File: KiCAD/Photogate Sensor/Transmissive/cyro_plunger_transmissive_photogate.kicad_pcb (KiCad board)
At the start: 2 copper layers, 100 x 100 mm, 0 parts

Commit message: Finish draft of schematic, started on board
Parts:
- added C1: 1µF, Capacitor_SMD:C_0805_2012Metric, F.Cu at (140.8, -2.38)
- added C2: 4.7µF, Capacitor_SMD:C_0805_2012Metric, F.Cu at (140.8, 0.63)
- added C3: 100nF, Capacitor_SMD:C_0805_2012Metric, F.Cu at (140.8, 3.64)
- added C4: 100nF, Capacitor_SMD:C_0805_2012Metric, F.Cu at (27.8, 25.0)
- added C5: 100nF, Capacitor_SMD:C_0805_2012Metric, F.Cu at (140.8, 9.66)
- added C6: 100nF, Capacitor_SMD:C_0805_2012Metric, F.Cu at (9.71, 14.1)
- added C7: 100nF, Capacitor_SMD:C_0805_2012Metric, F.Cu at (9.71, 17.4)
- added D1: LED, LED_THT:LED_D5.0mm_Horizontal_O1.27mm_Z9.0mm, F.Cu at (141.0, 19.0)
- added D2: D_Schottky, Diode_SMD:D_SOD-323, F.Cu at (138.2, 52.0)
- added D4: D_Schottky, Diode_SMD:D_SOD-323, F.Cu at (140.7, 34.1)
- added D5: D, Diode_SMD:D_SOD-323, F.Cu at (20.7, 20.9)
- added D6: D_Schottky, Diode_SMD:D_SOD-323, F.Cu at (10.7, 9.45)
- added D7: D_Schottky, Diode_SMD:D_SOD-323, F.Cu at (3.10, 39.9)
- added D8: D_Schottky, Diode_SMD:D_SOD-323, F.Cu at (128.2, 53.9)
- added D9: D_Schottky, Diode_SMD:D_SOD-323, F.Cu at (128.2, 56.8)
- added J2: FFC Socket, Custom:AMPHENOL_SFW8S-2STE1LF, F.Cu at (2.00, 8.57)
- added J3: USB_B_Micro, Custom:CUI_UJ2-MIBH-G-SMT-TR, F.Cu at (16.2, 6.46)
- added J4: UPDI socket, Connector_PinSocket_2.54mm:PinSocket_1x06_P2.54mm_Vertical_SMD_Pin1Right, F.Cu at (11.5, 22.4)
- added Q1: Q_NMOS_GSD, Package_TO_SOT_SMD:SOT-23-3, F.Cu at (-6.20, 41.2)
- added Q2: Q_NMOS_GSD, Package_TO_SOT_SMD:SOT-23-3, F.Cu at (145.6, 3.14)
- added Q3: Q_NMOS_GSD, Package_TO_SOT_SMD:SOT-23-3, F.Cu at (145.6, 7.77)
- added Q4: Q_NMOS_GSD, Package_TO_SOT_SMD:SOT-23-3, F.Cu at (145.6, 12.4)
- added R1: 47, Custom:RES_SMF5_TYCO_TYC, F.Cu at (3.00, 45.0)
- added R2: 47, Custom:RES_SMF5_TYCO_TYC, F.Cu at (80.8, 45.0)
- added R3: 47, Custom:RES_SMF5_TYCO_TYC, F.Cu at (-25.5, -4.10)
- added R4: 200k, Resistor_SMD:R_0805_2012Metric, F.Cu at (146.2, 49.2)
- added R5: 100, Resistor_SMD:R_1206_3216Metric, F.Cu at (121.1, 47.2)
- added R6: 470, Resistor_SMD:R_0805_2012Metric, F.Cu at (22.6, 19.0)
- added RN1: 4.7k, Resistor_SMD:R_Array_Convex_4x1206, F.Cu at (129.5, 35.6)
- added RN2: 4.7k, Resistor_SMD:R_Array_Convex_4x1206, F.Cu at (135.0, 35.6)
- added TH1: Thermistor, Resistor_SMD:R_0805_2012Metric, F.Cu at (3.10, 50.1)
- added TH2: Thermistor, Resistor_SMD:R_0805_2012Metric, F.Cu at (157.6, 6.44)
- added TH3: Thermistor, Resistor_SMD:R_0805_2012Metric, F.Cu at (157.6, 9.39)
- added TP1: TestPoint, TestPoint:TestPoint_Pad_D3.0mm, F.Cu at (148.6, 31.3)
- added TP2: TestPoint, TestPoint:TestPoint_Pad_D3.0mm, F.Cu at (148.6, 36.4)
- added TP3: TestPoint, TestPoint:TestPoint_Pad_D3.0mm, F.Cu at (153.6, 31.3)
- added TP4: TestPoint, TestPoint:TestPoint_Pad_D3.0mm, F.Cu at (153.6, 36.4)
- added TP5: TestPoint, TestPoint:TestPoint_Pad_D3.0mm, F.Cu at (158.7, 31.3)
- added TP6: TestPoint, TestPoint:TestPoint_Pad_D3.0mm, F.Cu at (158.7, 36.4)
- added U1: 5V LDO, Package_TO_SOT_SMD:SOT-223-3_TabPin2, F.Cu at (2.00, 15.3)
- added U2: Opamp_Dual, Package_SO:MSOP-8_3x3mm_P0.65mm, F.Cu at (38.0, 21.3)
- added U3: AD5242BRUZ1M, Custom:AD5242BRUZ1M, F.Cu at (122.3, 24.5)
- added U4: ATTiny1614, Package_SO:SOIC-14_3.9x8.7mm_P1.27mm, F.Cu at (28.0, 19.4)
- added U5: CH340C, Package_SO:SOP-16_3.9x9.9mm_P1.27mm, F.Cu at (15.9, 15.1)
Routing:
- net +5V: track 0.00 -> 31.1 mm
- net /Tx: track 0.00 -> 15.3 mm
- net +12V: track 0.00 -> 11.8 mm
- net /Rx: track 0.00 -> 11.5 mm
- net Net-(J3-D-): track 0.00 -> 8.92 mm
- net Net-(J3-D+): track 0.00 -> 8.86 mm
- net Net-(D6-A): track 0.00 -> 8.17 mm
- net Net-(U5-V3): track 0.00 -> 6.45 mm
- net /UPDI: track 0.00 -> 3.41 mm
- added copper zone on B.Cu, net GND
- added copper zone on F.Cu, net GND
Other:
- board size 100 x 100 mm -> 122 x 70 mm

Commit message: Analog and digital circuits mostly connected
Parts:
- R3: footprint Custom:RES_SMF5_TYCO_TYC -> Custom:RES_3550_TEC
- moved R3 262.3 mm to (173.5, 166.8)
- moved U1 245.1 mm to (198.8, 161.5), turned to 180 degrees
- moved D6 236.8 mm to (190.2, 163.8), turned to -90 degrees
- moved J3 232.7 mm to (184.7, 166.9), turned to 0 degrees
- moved C6 232.4 mm to (191.2, 159.2), turned to 90 degrees
- moved C7 228.2 mm to (191.2, 155.8), turned to 90 degrees
- moved J2 228.0 mm to (172.3, 160.1), turned to 180 degrees
- moved U5 221.5 mm to (185.0, 158.2), turned to -90 degrees
- moved J4 219.4 mm to (189.4, 150.8), turned to -90 degrees
- moved R6 205.2 mm to (178.5, 152.5), turned to 180 degrees
- moved D5 205.1 mm to (179.6, 150.5), turned to 180 degrees
- moved C4 194.9 mm to (173.2, 154.8)
- moved U4 194.0 mm to (172.2, 149.2)
- moved C2 167.0 mm to (193.3, 159.2), turned to 90 degrees
- moved C1 164.2 mm to (268.3, 101.1)
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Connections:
- net Net-(Q4-S) renamed /LED Isense
- C1 pad 2: Net-(U1-GND) -> GND
- C2 pad 2: Net-(U1-GND) -> GND
- D6 pad 2: Net-(D6-A) -> /Vusb
- J2 pad 1: +12V -> /D+
- J2 pad 2: GND -> /D-
- J2 pad 8: GND -> /Vusb
- J3 pad 1: Net-(D6-A) -> /Vusb
- J3 pad 2: Net-(J3-D-) -> /D-
- J3 pad 3: Net-(J3-D+) -> /D+
- J4 pad 1: +5V -> /Vusb
- J4 pad 2: +5V -> /Vusb
- RN1 pad 1: unconnected-(RN1-R1.1-Pad1) -> /Therm3
- RN1 pad 2: /Therm3 -> /Therm2
- RN1 pad 3: /Therm2 -> /Therm1
- RN1 pad 4: /Therm1 -> unconnected-(RN1-R4.1-Pad4)
- RN1 pad 5: +5V -> unconnected-(RN1-R4.2-Pad5)
- RN1 pad 8: unconnected-(RN1-R1.2-Pad8) -> +5V
- TH2 pad 2: /Therm1 -> /Therm2
- TH3 pad 2: /Therm1 -> /Therm3
- TP3 pad 1: /Vled-ref+ -> unconnected-(TP3-Pad1)
- TP4 pad 1: /Vled-ref- -> unconnected-(TP4-Pad1)
- U1 pad 1: Net-(U1-GND) -> GND
- U4 pad 11: /Therm3 -> /Therm1
- U4 pad 13: /Therm1 -> /Therm3
- U4 pad 2: /Heater1 -> /Heater3
- U4 pad 7: /Heater3 -> /Heater1
- U5 pad 5: Net-(J3-D+) -> /D+
- U5 pad 6: Net-(J3-D-) -> /D-
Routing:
- net GND: track 0.00 -> 222.4 mm, vias 0 -> 230
- net +12V: track 11.8 -> 160.3 mm
- net /Therm1: track 0.00 -> 93.1 mm
- net +5V: track 31.1 -> 110.7 mm, vias 0 -> 6
- net /Heater1: track 0.00 -> 74.0 mm
- net /Photo_output: track 0.00 -> 71.9 mm
- net /Vusb: track 0.00 -> 58.8 mm
- net /SCL: track 0.00 -> 45.6 mm
- net /SDA: track 0.00 -> 44.7 mm
- net /Comp Out: track 0.00 -> 30.1 mm
- net /Therm3: track 0.00 -> 26.3 mm
- net /D-: track 0.00 -> 25.3 mm
- net /D+: track 0.00 -> 24.7 mm
- net /Heater3: track 0.00 -> 22.8 mm
- net Net-(D7-A): track 0.00 -> 13.2 mm
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- added copper zone on F.Cu, net +12V
- added copper zone on F.Cu, net +5V
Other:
- outline, holes or cut-outs redrawn

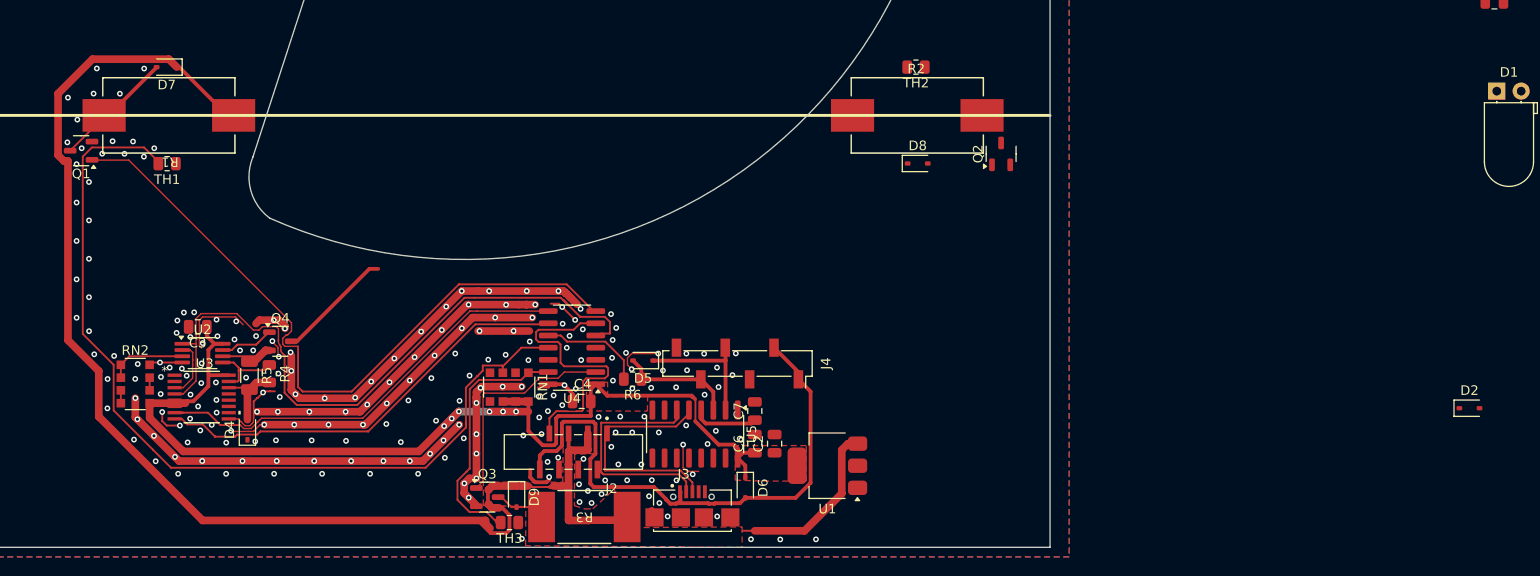
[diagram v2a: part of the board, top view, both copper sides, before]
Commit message: More connections
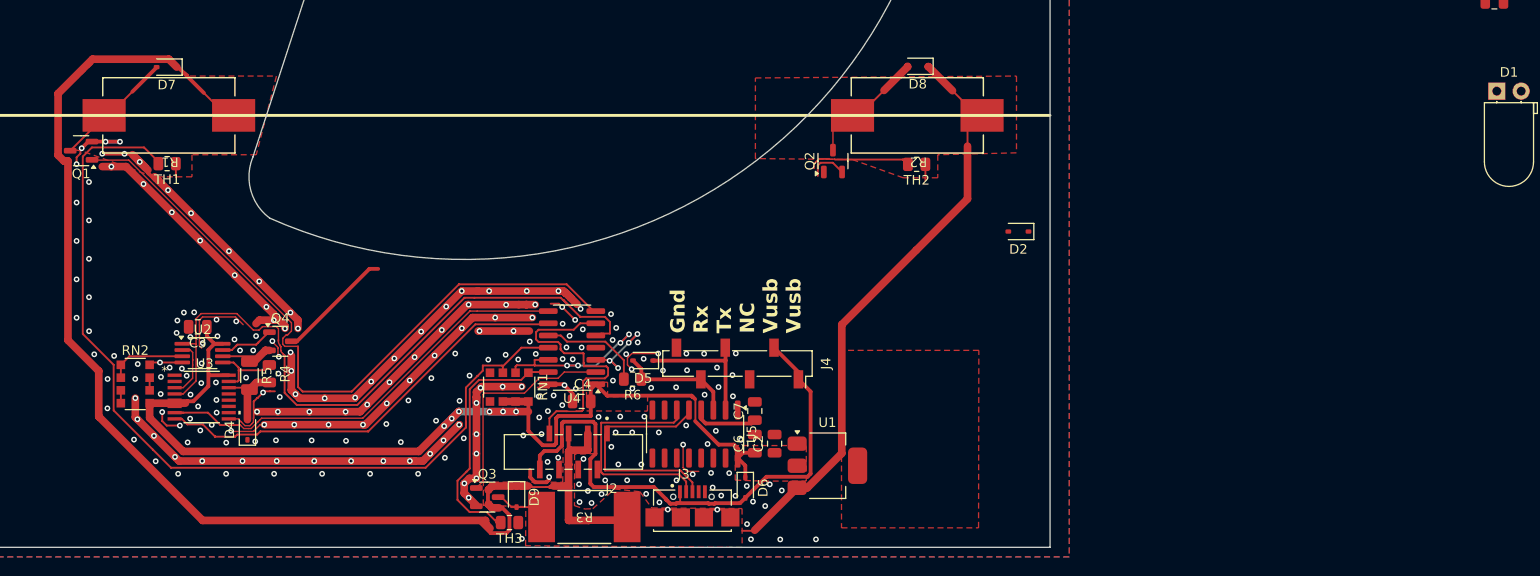
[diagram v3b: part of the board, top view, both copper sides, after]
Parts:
- moved D2 50.5 mm to (218.7, 137.1), turned to 180 degrees
- moved Q2 17.5 mm to (199.4, 129.8)
- moved TH2 10.1 mm to (208.1, 130.1)
- moved D8 10.1 mm to (208.2, 119.9), turned to 180 degrees
- turned R2 to 180 degrees
- turned U1 to 0 degrees
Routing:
- net GND: track 222.4 -> 301.2 mm, vias 230 -> 250
- net +12V: track 160.3 -> 205.1 mm
- net /Therm2: track 0.21 -> 29.5 mm, vias 0 -> 4
- net Net-(D8-A): track 0.00 -> 12.5 mm
- net /Heater2: track 0.00 -> 9.20 mm, vias 0 -> 4
- net /Vusb: track 58.8 -> 58.1 mm
- added copper zone on F.Cu, net /Therm1
- added copper zone on F.Cu, net /Therm2
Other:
- board text added: "Gnd Rx Tx NC Vusb Vusb"

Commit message: More path optimization
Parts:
- moved C5 146.2 mm to (129.2, 158.1)
- moved C1 84.5 mm to (208.2, 160.5), turned to -90 degrees
- moved D2 73.8 mm to (145.9, 149.1), turned to -90 degrees
- moved D1 29.9 mm to (239.5, 129.5), turned to -90 degrees
- moved U1 3.89 mm to (202.5, 160.3), turned to 180 degrees
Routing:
- net GND: track 301.2 -> 461.0 mm, vias 250 -> 425
- net +5V: track 110.7 -> 181.8 mm, vias 6 -> 12
- net Net-(D1-K): track 12.2 -> 53.5 mm
- net /Heater2: track 9.20 -> 44.3 mm
- net /Therm2: track 29.5 -> 58.7 mm
- net /Vusb: track 58.1 -> 80.0 mm
- net +12V: track 205.1 -> 216.1 mm
- net /W1: track 6.17 -> 9.56 mm
- net Net-(D7-A): track 13.7 -> 15.7 mm
- net Net-(U5-V3): track 7.59 -> 9.29 mm
- net /D+: track 24.7 -> 25.3 mm
- net /Therm1: track 93.1 -> 92.5 mm

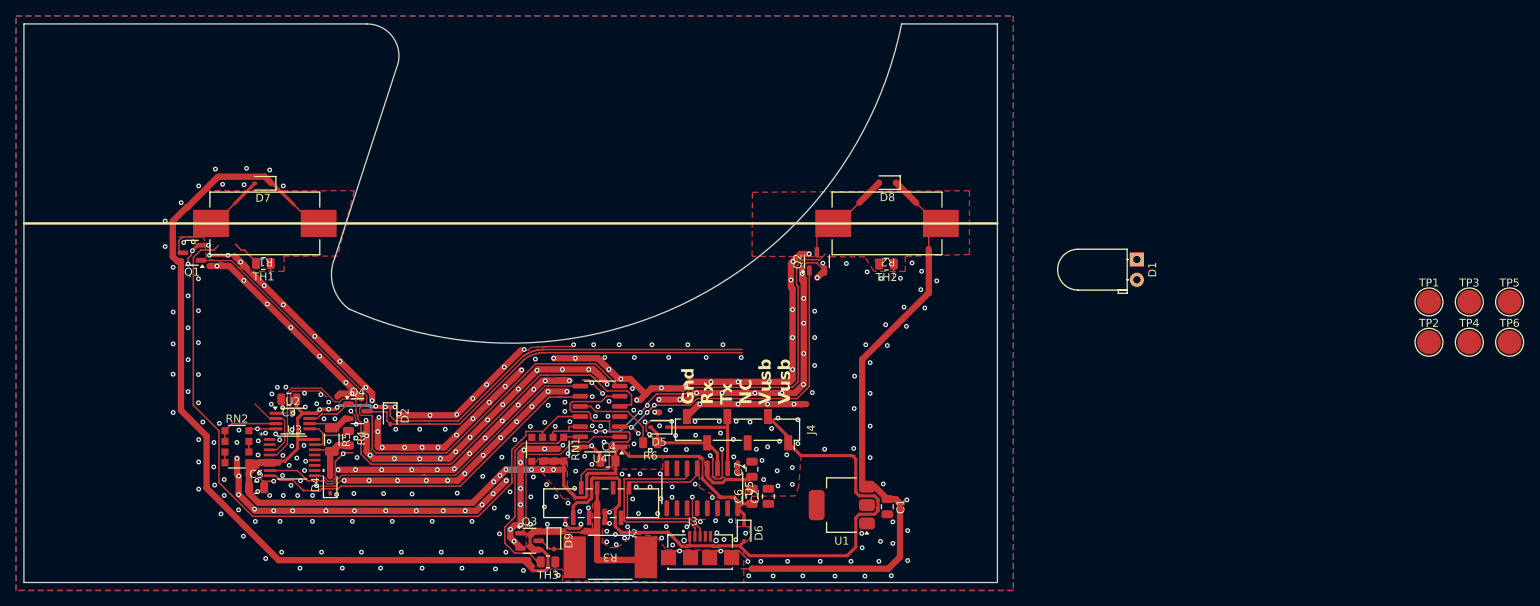
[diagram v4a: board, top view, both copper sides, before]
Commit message: Add RC filter and I2C breakout - passes DRC
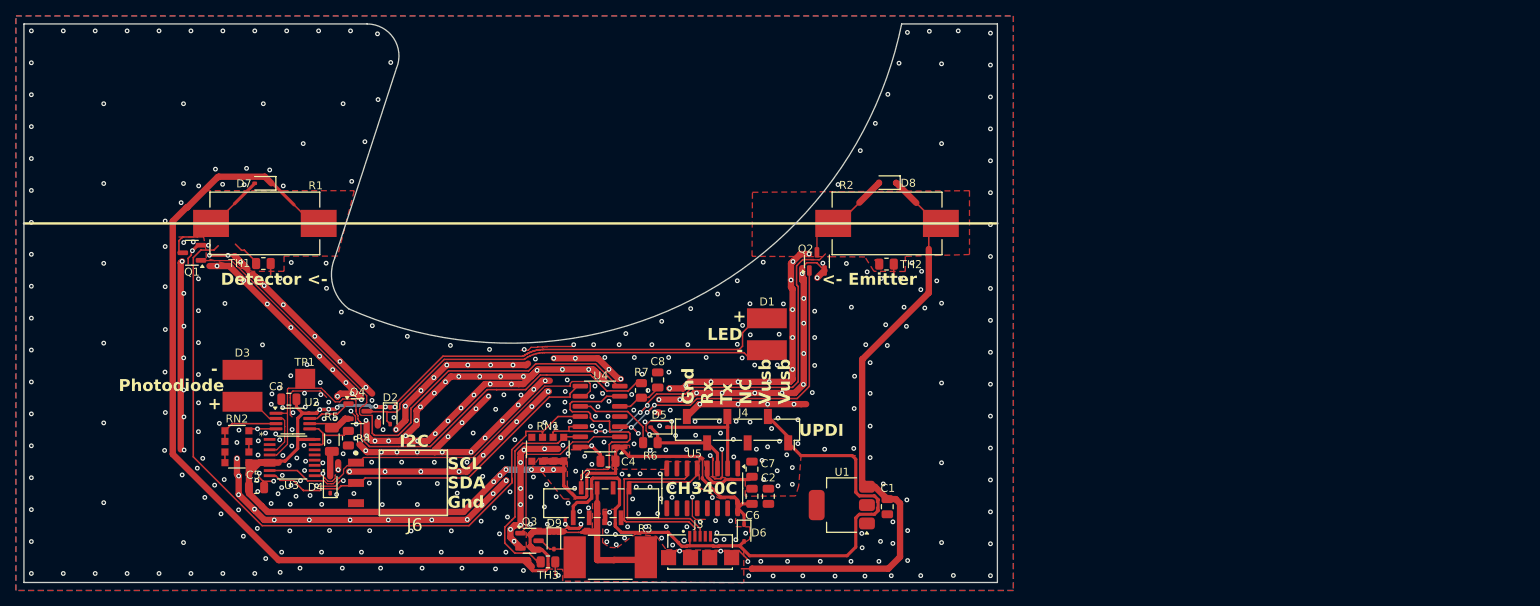
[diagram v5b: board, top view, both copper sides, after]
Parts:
- removed TP2, TP3, TP4, TP5, TP6: TestPoint, TestPoint:TestPoint_Pad_D3.0mm
- added C8: 100nF, Capacitor_SMD:C_0805_2012Metric, F.Cu at (179.4, 144.6)
- added D3: D_Photo, Custom:Solder pads, F.Cu at (127.4, 145.3)
- added J6: Conn_01x03_Socket, Custom:GCT_BG300-03-X-X-A_REVC, F.Cu at (146.8, 157.5)
- added R7: 470, Resistor_SMD:R_0805_2012Metric, F.Cu at (177.4, 145.9)
- D1: footprint LED_THT:LED_D5.0mm_Horizontal_O1.27mm_Z9.0mm -> Custom:Solder pads
- TP1: footprint TestPoint:TestPoint_Pad_D3.0mm -> Custom:1x Solder pads
- moved TP1 141.2 mm to (135.2, 144.5)
- moved D1 47.3 mm to (193.1, 138.9), turned to 180 degrees
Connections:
- D4 pad 2: /Vled-ref- -> Net-(D4-A)
- R4 pad 2: /Vled-ref- -> GND
- R5 pad 2: /Vled-ref- -> Net-(D4-A)
- U3 pad 14: /Vled-ref- -> GND
- U4 pad 5: /Photo_output -> /Filtered_output
- U4 pad 8: /SCL -> /SDA
- U4 pad 9: /SDA -> /SCL
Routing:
- net /Vled-ref-: track 8.08 -> 0.00 mm
- net /Filtered_output: track 0.00 -> 6.37 mm
- net /Photo_output: track 72.1 -> 67.2 mm
- net +5V: track 181.8 -> 186.0 mm
- net Net-(D4-A): track 0.00 -> 3.74 mm
- net /SCL: track 46.1 -> 48.3 mm
- net /Heater1: track 74.0 -> 72.1 mm
- net GND: track 461.0 -> 462.2 mm, vias 425 -> 562
- net Net-(D1-K): track 53.5 -> 54.5 mm
- net /Therm1: track 92.5 -> 93.5 mm
- net /SDA: track 44.7 -> 45.3 mm
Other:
- board text added: "+"
- board text added: "-"
- board text added: "<- Emitter"
- board text added: "CH340C"
- board text added: "Detector <-"
- board text added: "I2C"
- board text added: "LED"
- board text added: "Photodiode"
- board text added: "SCL SDA Gnd"
- board text added: "UPDI"

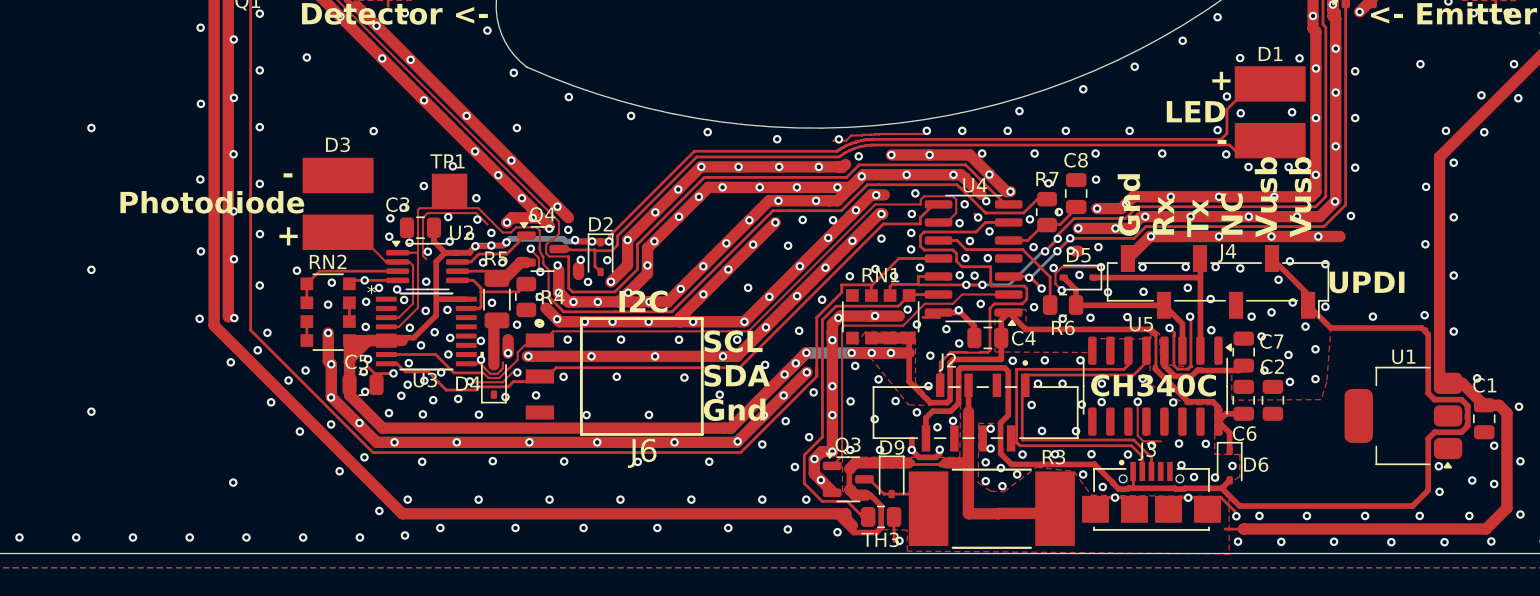
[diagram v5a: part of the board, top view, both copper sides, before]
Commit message: Add digipot bypass - upgrade to moisture resistance when possible
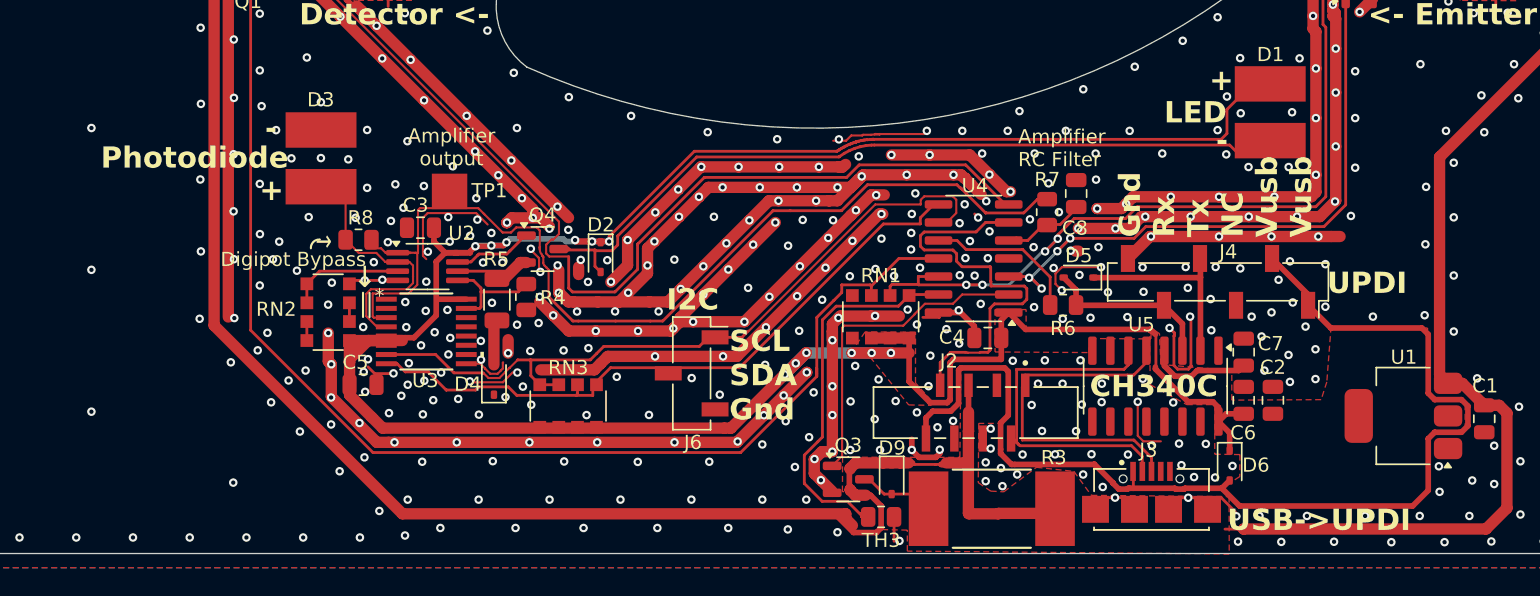
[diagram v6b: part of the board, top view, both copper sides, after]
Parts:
- added R8: 2M, Resistor_SMD:R_0805_2012Metric, F.Cu at (128.8, 147.9)
- added RN3: 4.7k, Resistor_SMD:R_Array_Convex_4x1206, F.Cu at (143.6, 159.6)
- C1: value 1µF -> 4.7µF
- J6: footprint Custom:GCT_BG300-03-X-X-A_REVC -> Connector_PinSocket_2.54mm:PinSocket_1x03_P2.54mm_Vertical_SMD_Pin1Right
- moved J6 5.48 mm to (152.3, 157.3), turned to 0 degrees
- moved D3 3.43 mm to (126.2, 142.1)
- turned C3 to 0 degrees
- turned C4 to 180 degrees
- turned C5 to 180 degrees
- turned C6 to -90 degrees
- turned C7 to -90 degrees
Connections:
- C3 pad 1: +5V -> GND
- C3 pad 2: GND -> +5V
- C4 pad 1: GND -> +5V
- C4 pad 2: +5V -> GND
- C5 pad 1: +5V -> GND
- C5 pad 2: GND -> +5V
- C6 pad 1: +5V -> GND
- C6 pad 2: GND -> +5V
- C7 pad 1: Net-(U5-V3) -> GND
- C7 pad 2: GND -> Net-(U5-V3)
- D3 pad 1: /W1 -> /Photo_current
- R7 pad 1: /Photo_output -> /Amplifier_output
- TP1 pad 1: /Photo_output -> /Amplifier_output
- U2 pad 1: /Photo_output -> /Amplifier_output
- U2 pad 2: /W1 -> /Photo_current
- U3 pad 3: /W1 -> /Amplifier_output
- U3 pad 4: /Photo_output -> /Photo_current
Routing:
- net /Amplifier_output: track 0.00 -> 71.7 mm
- net /Photo_output: track 67.2 -> 0.00 mm
- net /Photo_current: track 0.00 -> 17.8 mm
- net /W1: track 9.56 -> 0.00 mm
- net /SCL: track 48.3 -> 52.6 mm
- net /SDA: track 45.3 -> 46.9 mm
- net GND: track 462.2 -> 462.8 mm, vias 562 -> 571
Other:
- board text added: "Amplifier RC Filter"
- board text added: "Amplifier output"
- board text added: "Digipot Bypass"
- board text added: "USB->UPDI"
- board text added: "↓"
